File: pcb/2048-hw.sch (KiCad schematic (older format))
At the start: 41 parts

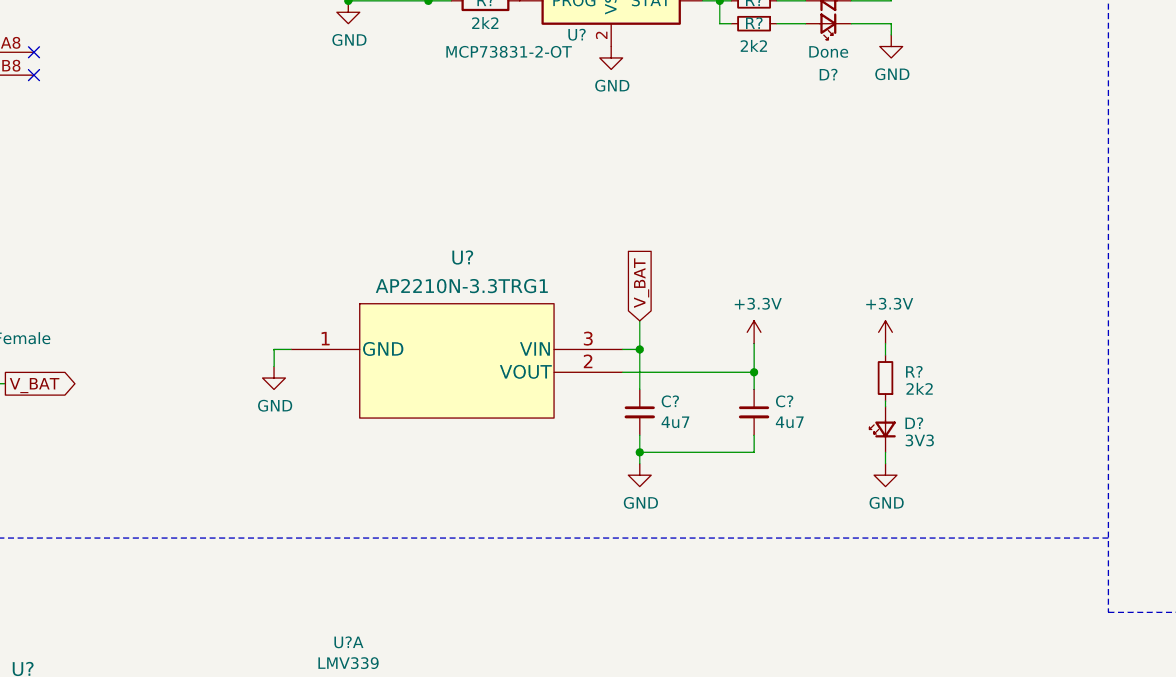
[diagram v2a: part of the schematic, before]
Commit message: Add battery ADC voltage divider
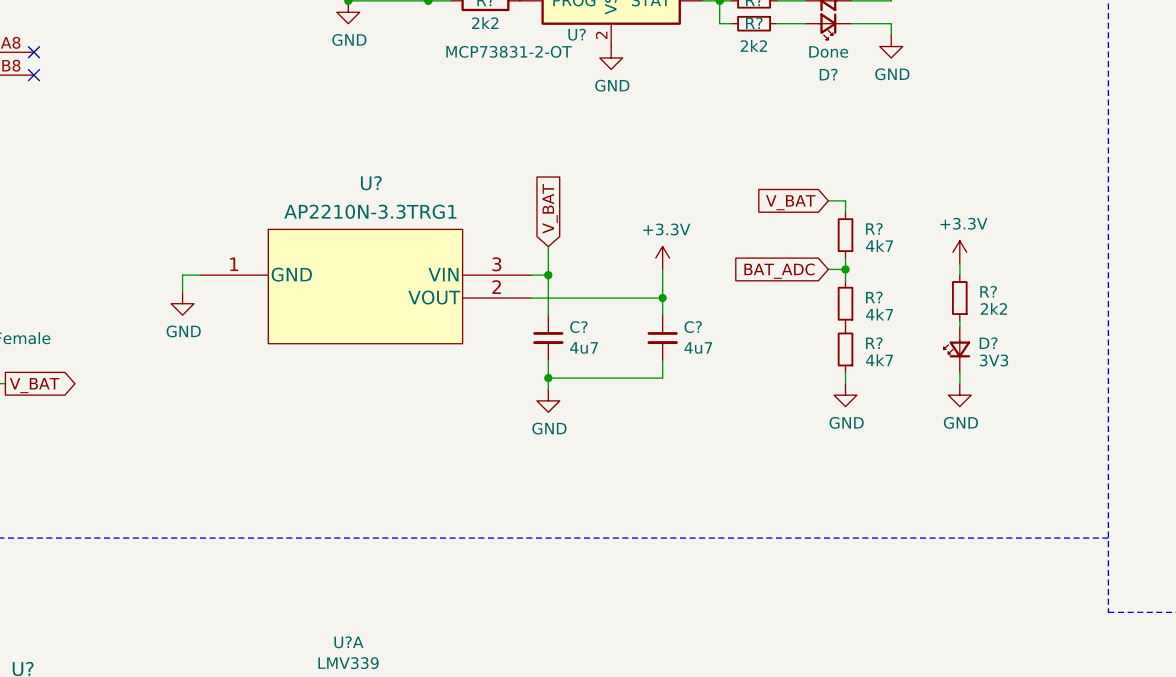
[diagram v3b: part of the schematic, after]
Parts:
- added R? (x3): 4k7, symbol Device:R_Small
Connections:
- net BAT_ADC: now also R?.1, R?.2
- net GND: now also R?.1
- net V_BAT: now also R?.2
- new net: R?.1, R?.2
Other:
- moved on the sheet: C?, D?, R?, U?
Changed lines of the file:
@@
 	1100 3500 1100 3800
 Wire Wire Line
-	2975 3500 2975 3575
-Wire Wire Line
-	3050 3500 2975 3500
-Connection ~ 5075 3600
-Wire Wire Line
-	5075 3600 5075 3475
-Wire Wire Line
-	4575 3950 4575 4000
-Connection ~ 4575 3950
-Wire Wire Line
-	5075 3875 5075 3950
-Wire Wire Line
-	5075 3950 4575 3950
-Wire Wire Line
-	5075 3600 5075 3675
-Wire Wire Line
-	4500 3600 5075 3600
-Wire Wire Line
-	4575 3875 4575 3950
-Wire Wire Line
-	4575 3500 4575 3675
-Wire Wire Line
-	4500 3500 4575 3500
+	2575 3175 2575 3250
+Wire Wire Line
+	2650 3175 2575 3175
+Connection ~ 4675 3275
+Wire Wire Line
+	4675 3275 4675 3150
+Wire Wire Line
+	4175 3625 4175 3675
+Connection ~ 4175 3625
+Wire Wire Line
+	4675 3550 4675 3625
+Wire Wire Line
+	4675 3625 4175 3625
+Wire Wire Line
+	4675 3275 4675 3350
+Wire Wire Line
+	4100 3275 4675 3275
+Wire Wire Line
+	4175 3550 4175 3625
+Wire Wire Line
+	4175 3175 4175 3350
+Wire Wire Line
+	4100 3175 4175 3175
 $Comp
 L power:+3.3V #PWR0112
 U 1 1 5FEF81B7
-P 5075 3475
-F 0 "#PWR0112" H 5075 3325 50  0001 C CNN
-F 1 "+3.3V" H 5090 3648 50  0000 C CNN
-F 2 "" H 5075 3475 50  0001 C CNN
-F 3 "" H 5075 3475 50  0001 C CNN
-	1    5075 3475
+P 4675 3150
+F 0 "#PWR0112" H 4675 3000 50  0001 C CNN
+F 1 "+3.3V" H 4690 3323 50  0000 C CNN
+F 2 "" H 4675 3150 50  0001 C CNN
+F 3 "" H 4675 3150 50  0001 C CNN
+	1    4675 3150
 	1    0    0    -1
 $EndComp
@@
 L power:GND #PWR0113
 U 1 1 5FEF771E
-P 4575 4000
-F 0 "#PWR0113" H 4575 3750 50  0001 C CNN
-F 1 "GND" H 4580 3827 50  0000 C CNN
-F 2 "" H 4575 4000 50  0001 C CNN
-F 3 "" H 4575 4000 50  0001 C CNN
-	1    4575 4000
+P 4175 3675
+F 0 "#PWR0113" H 4175 3425 50  0001 C CNN
+F 1 "GND" H 4180 3502 50  0000 C CNN
+F 2 "" H 4175 3675 50  0001 C CNN
+F 3 "" H 4175 3675 50  0001 C CNN
+	1    4175 3675
 	1    0    0    -1
 $EndComp
@@
 L Device:C_Small C?
 U 1 1 5FEF733E
-P 5075 3775
-F 0 "C?" H 5167 3821 50  0000 L CNN
-F 1 "4u7" H 5167 3730 50  0000 L CNN
-F 2 "" H 5075 3775 50  0001 C CNN
-F 3 "~" H 5075 3775 50  0001 C CNN
-	1    5075 3775
+P 4675 3450
+F 0 "C?" H 4767 3496 50  0000 L CNN
+F 1 "4u7" H 4767 3405 50  0000 L CNN
+F 2 "" H 4675 3450 50  0001 C CNN
+F 3 "~" H 4675 3450 50  0001 C CNN
+	1    4675 3450
 	1    0    0    -1
 $EndComp
@@
 L Device:C_Small C?
 U 1 1 5FEF6AD9
-P 4575 3775
-F 0 "C?" H 4667 3821 50  0000 L CNN
-F 1 "4u7" H 4667 3730 50  0000 L CNN
-F 2 "" H 4575 3775 50  0001 C CNN
-F 3 "~" H 4575 3775 50  0001 C CNN
-	1    4575 3775
+P 4175 3450
+F 0 "C?" H 4267 3496 50  0000 L CNN
+F 1 "4u7" H 4267 3405 50  0000 L CNN
+F 2 "" H 4175 3450 50  0001 C CNN
+F 3 "~" H 4175 3450 50  0001 C CNN
+	1    4175 3450
 	1    0    0    -1
 $EndComp
@@
 L power:GND #PWR0114
 U 1 1 5FEF6103
-P 2975 3575
-F 0 "#PWR0114" H 2975 3325 50  0001 C CNN
-F 1 "GND" H 2980 3402 50  0000 C CNN
-F 2 "" H 2975 3575 50  0001 C CNN
-F 3 "" H 2975 3575 50  0001 C CNN
-	1    2975 3575
+P 2575 3250
+F 0 "#PWR0114" H 2575 3000 50  0001 C CNN
+F 1 "GND" H 2580 3077 50  0000 C CNN
+F 2 "" H 2575 3250 50  0001 C CNN
+F 3 "" H 2575 3250 50  0001 C CNN
+	1    2575 3250
 	1    0    0    -1
 $EndComp
@@
 L ap2210:AP2210N-3.3TRG1 U?
 U 1 1 5FEF5741
-P 3050 3500
-F 0 "U?" H 3800 3900 60  0000 C CNN
-F 1 "AP2210N-3.3TRG1" H 3800 3775 60  0000 C CNN
-F 2 "SOT_3.3TRG1_DIO" H 3850 3740 60  0001 C CNN
-F 3 "" H 3050 3500 60  0000 C CNN
-	1    3050 3500
+P 2650 3175
+F 0 "U?" H 3400 3575 60  0000 C CNN
+F 1 "AP2210N-3.3TRG1" H 3400 3450 60  0000 C CNN
+F 2 "SOT_3.3TRG1_DIO" H 3450 3415 60  0001 C CNN
+F 3 "" H 2650 3175 60  0000 C CNN
+	1    2650 3175
 	1    0    0    -1
 $EndComp
@@
 L power:+3.3V #PWR0115
 U 1 1 5FF1A477
-P 5650 3475
-F 0 "#PWR0115" H 5650 3325 50  0001 C CNN
-F 1 "+3.3V" H 5665 3648 50  0000 C CNN
-F 2 "" H 5650 3475 50  0001 C CNN
-F 3 "" H 5650 3475 50  0001 C CNN
-	1    5650 3475
+P 5975 3125
+F 0 "#PWR0115" H 5975 2975 50  0001 C CNN
+F 1 "+3.3V" H 5990 3298 50  0000 C CNN
+F 2 "" H 5975 3125 50  0001 C CNN
+F 3 "" H 5975 3125 50  0001 C CNN
+	1    5975 3125
 	1    0    0    -1
 $EndComp
@@
 L Device:R_Small R?
 U 1 1 5FF1A977
-P 5650 3625
-F 0 "R?" H 5525 3600 50  0000 C CNN
-F 1 "2k2" H 5500 3675 50  0000 C CNN
-F 2 "" H 5650 3625 50  0001 C CNN
-F 3 "~" H 5650 3625 50  0001 C CNN
-	1    5650 3625
+P 5975 3275
+F 0 "R?" H 5850 3250 50  0000 C CNN
+F 1 "2k2" H 5825 3325 50  0000 C CNN
+F 2 "" H 5975 3275 50  0001 C CNN
+F 3 "~" H 5975 3275 50  0001 C CNN
+	1    5975 3275
 	-1   0    0    1
 $EndComp
@@
 L Device:LED_Small D?
 U 1 1 5FF1B0E2
-P 5650 3850
-F 0 "D?" V 5675 3725 50  0000 C CNN
-F 1 "3V3" V 5600 3700 50  0000 C CNN
-F 2 "" V 5650 3850 50  0001 C CNN
-F 3 "~" V 5650 3850 50  0001 C CNN
-	1    5650 3850
+P 5975 3500
+F 0 "D?" V 6000 3375 50  0000 C CNN
+F 1 "3V3" V 5925 3350 50  0000 C CNN
+F 2 "" V 5975 3500 50  0001 C CNN
+F 3 "~" V 5975 3500 50  0001 C CNN
+	1    5975 3500
 	0    -1   -1   0
 $EndComp
@@
 L power:GND #PWR0116
 U 1 1 5FF1BC0E
-P 5650 4000
-F 0 "#PWR0116" H 5650 3750 50  0001 C CNN
-F 1 "GND" H 5655 3827 50  0000 C CNN
-F 2 "" H 5650 4000 50  0001 C CNN
-F 3 "" H 5650 4000 50  0001 C CNN
-	1    5650 4000
-	1    0    0    -1
-$EndComp
-Text GLabel 4575 3375 1    50   Input ~ 0
+P 5975 3650
+F 0 "#PWR0116" H 5975 3400 50  0001 C CNN
+F 1 "GND" H 5980 3477 50  0000 C CNN
+F 2 "" H 5975 3650 50  0001 C CNN
+F 3 "" H 5975 3650 50  0001 C CNN
+	1    5975 3650
+	1    0    0    -1
+$EndComp
+Text GLabel 4175 3050 1    50   Input ~ 0
 V_BAT
 Wire Wire Line
-	4575 3500 4575 3375
-Connection ~ 4575 3500
-Wire Wire Line
-	5650 3475 5650 3525
-Wire Wire Line
-	5650 3725 5650 3750
-Wire Wire Line
-	5650 3950 5650 4000
+	4175 3175 4175 3050
+Connection ~ 4175 3175
+Wire Wire Line
+	5975 3125 5975 3175
+Wire Wire Line
+	5975 3375 5975 3400
+Wire Wire Line
+	5975 3600 5975 3650
 $Comp
 L MCU_ST_STM32F3:STM32F303K8Tx U?
@@
 Wire Notes Line
 	6625 475  6625 4650
+$Comp
+L Device:R_Small R?
+U 1 1 5FFE2625
+P 5475 3000
+F 0 "R?" H 5350 2975 50  0000 C CNN
+F 1 "4k7" H 5325 3050 50  0000 C CNN
+F 2 "" H 5475 3000 50  0001 C CNN
+F 3 "~" H 5475 3000 50  0001 C CNN
+	1    5475 3000
+	-1   0    0    1
+$EndComp
+$Comp
+L power:GND #PWR?
+U 1 1 5FFE2631
+P 5475 3650
+F 0 "#PWR?" H 5475 3400 50  0001 C CNN
+F 1 "GND" H 5480 3477 50  0000 C CNN
+F 2 "" H 5475 3650 50  0001 C CNN
+F 3 "" H 5475 3650 50  0001 C CNN
+	1    5475 3650
+	1    0    0    -1
+$EndComp
+$Comp
+L Device:R_Small R?
+U 1 1 5FFEB48F
+P 5475 3300
+F 0 "R?" H 5350 3275 50  0000 C CNN
+F 1 "4k7" H 5325 3350 50  0000 C CNN
+F 2 "" H 5475 3300 50  0001 C CNN
+F 3 "~" H 5475 3300 50  0001 C CNN
+	1    5475 3300
+	-1   0    0    1
+$EndComp
+$Comp
+L Device:R_Small R?
+U 1 1 5FFEB927
+P 5475 3500
+F 0 "R?" H 5350 3475 50  0000 C CNN
+F 1 "4k7" H 5325 3550 50  0000 C CNN
+F 2 "" H 5475 3500 50  0001 C CNN
+F 3 "~" H 5475 3500 50  0001 C CNN
+	1    5475 3500
+	-1   0    0    1
+$EndComp
+Wire Wire Line
+	5475 3650 5475 3600
+Wire Wire Line
+	5475 3100 5475 3150
+Text GLabel 5400 2850 0    50   Input ~ 0
+V_BAT
+Text GLabel 5400 3150 0    50   Input ~ 0
+BAT_ADC
+Wire Wire Line
+	5400 2850 5475 2850
+Wire Wire Line
+	5400 3150 5475 3150
+Connection ~ 5475 3150
+Wire Wire Line
+	5475 3150 5475 3200
+Wire Wire Line
+	5475 2850 5475 2900
 $EndSCHEMATC

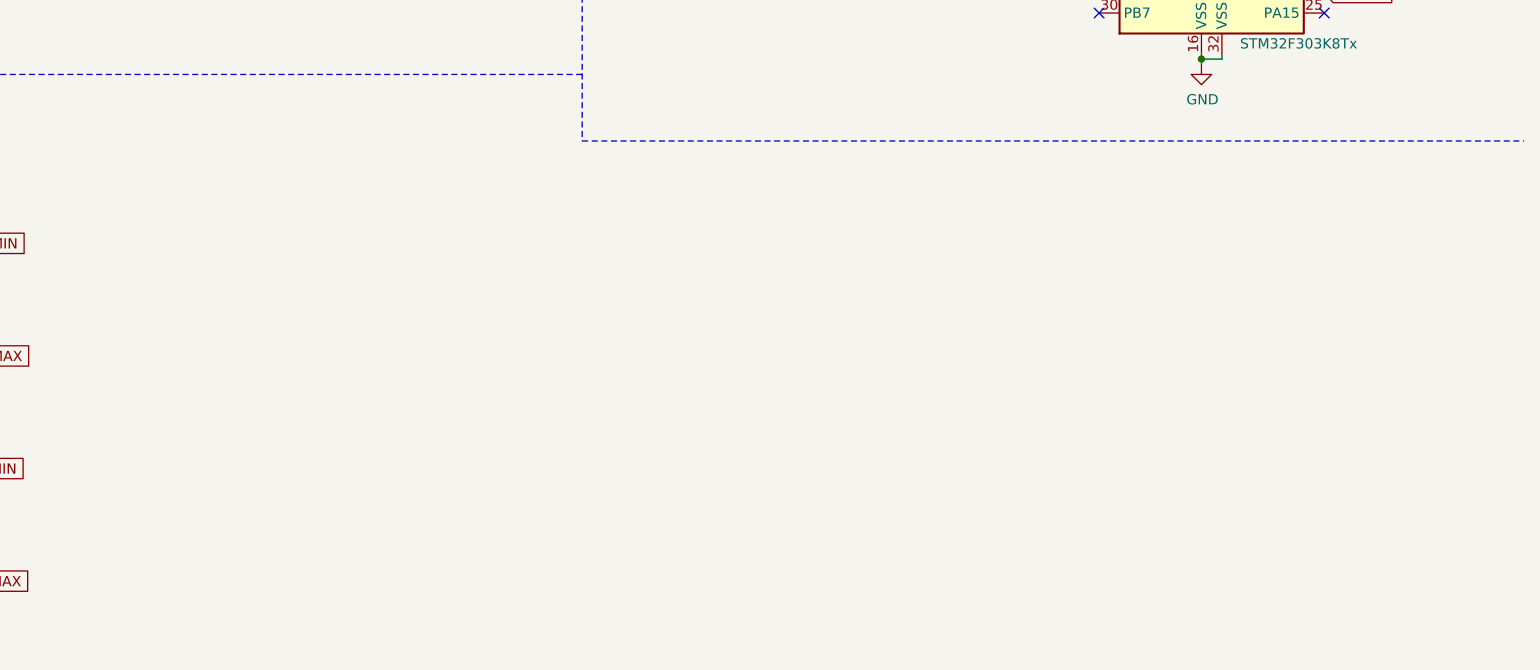
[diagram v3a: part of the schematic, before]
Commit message: Add ws2812b LEDs
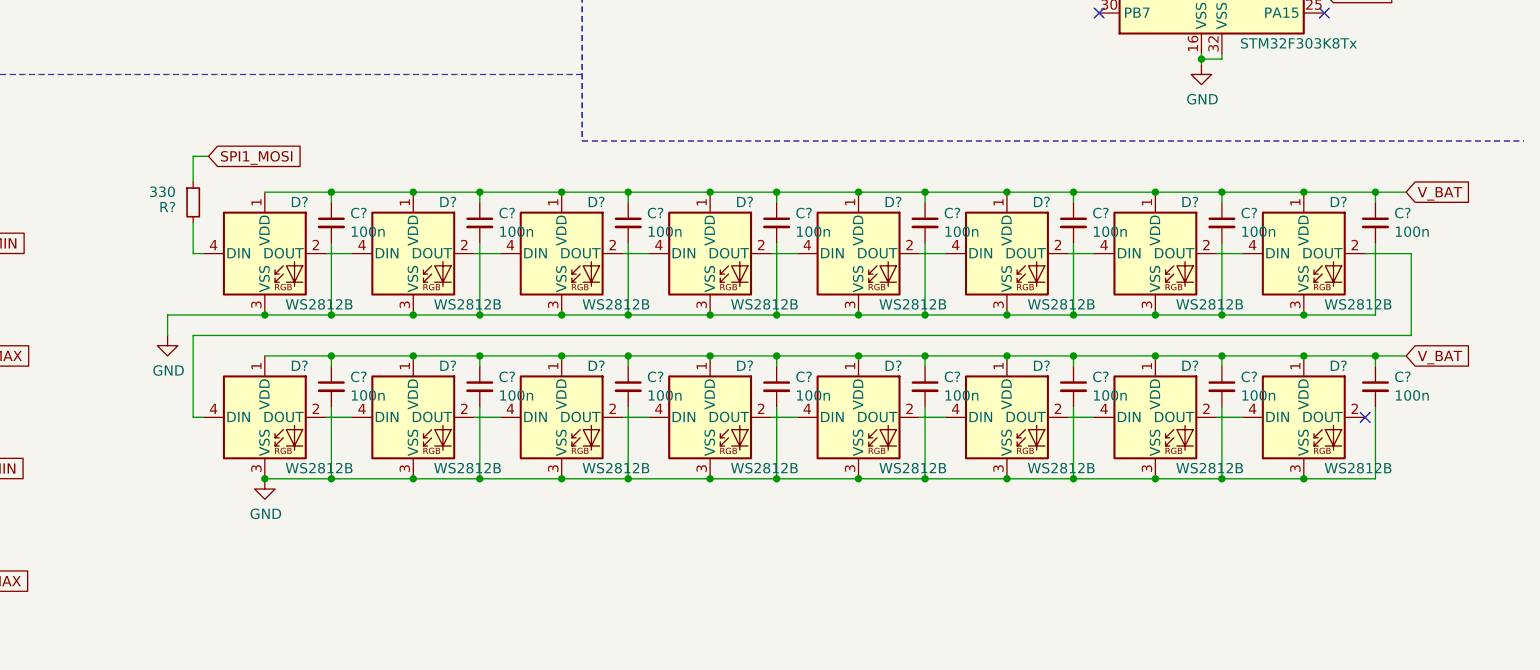
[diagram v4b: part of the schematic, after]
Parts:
- added C? (x16): 100n, symbol Device:C_Small
- added D? (x16): WS2812B, LED_SMD:LED_WS2812B_PLCC4_5.0x5.0mm_P3.2mm, symbol LED:WS2812B
- added R?: 330, symbol Device:R_Small
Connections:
- net GND: now also C?.2, C?.2, C?.2, C?.2, C?.2, C?.2, C?.2, C?.2, C?.2, C?.2, C?.2, C?.2, C?.2, C?.2, C?.2, C?.2, D?.3 (VSS), D?.3 (VSS), D?.3 (VSS), D?.3 (VSS), D?.3 (VSS), D?.3 (VSS), D?.3 (VSS), D?.3 (VSS), D?.3 (VSS), D?.3 (VSS), D?.3 (VSS), D?.3 (VSS), D?.3 (VSS), D?.3 (VSS), D?.3 (VSS), D?.3 (VSS)
- net SPI1_MOSI: now also R?.1
- net V_BAT: now also C?.1, C?.1, C?.1, C?.1, C?.1, C?.1, C?.1, C?.1, C?.1, C?.1, C?.1, C?.1, C?.1, C?.1, C?.1, C?.1, D?.1 (VDD), D?.1 (VDD), D?.1 (VDD), D?.1 (VDD), D?.1 (VDD), D?.1 (VDD), D?.1 (VDD), D?.1 (VDD), D?.1 (VDD), D?.1 (VDD), D?.1 (VDD), D?.1 (VDD), D?.1 (VDD), D?.1 (VDD), D?.1 (VDD), D?.1 (VDD)
- new net: D?.2 (DOUT), D?.4 (DIN) (x15)
- new net: D?.4 (DIN), R?.2
- no-connect marks 13 -> 14

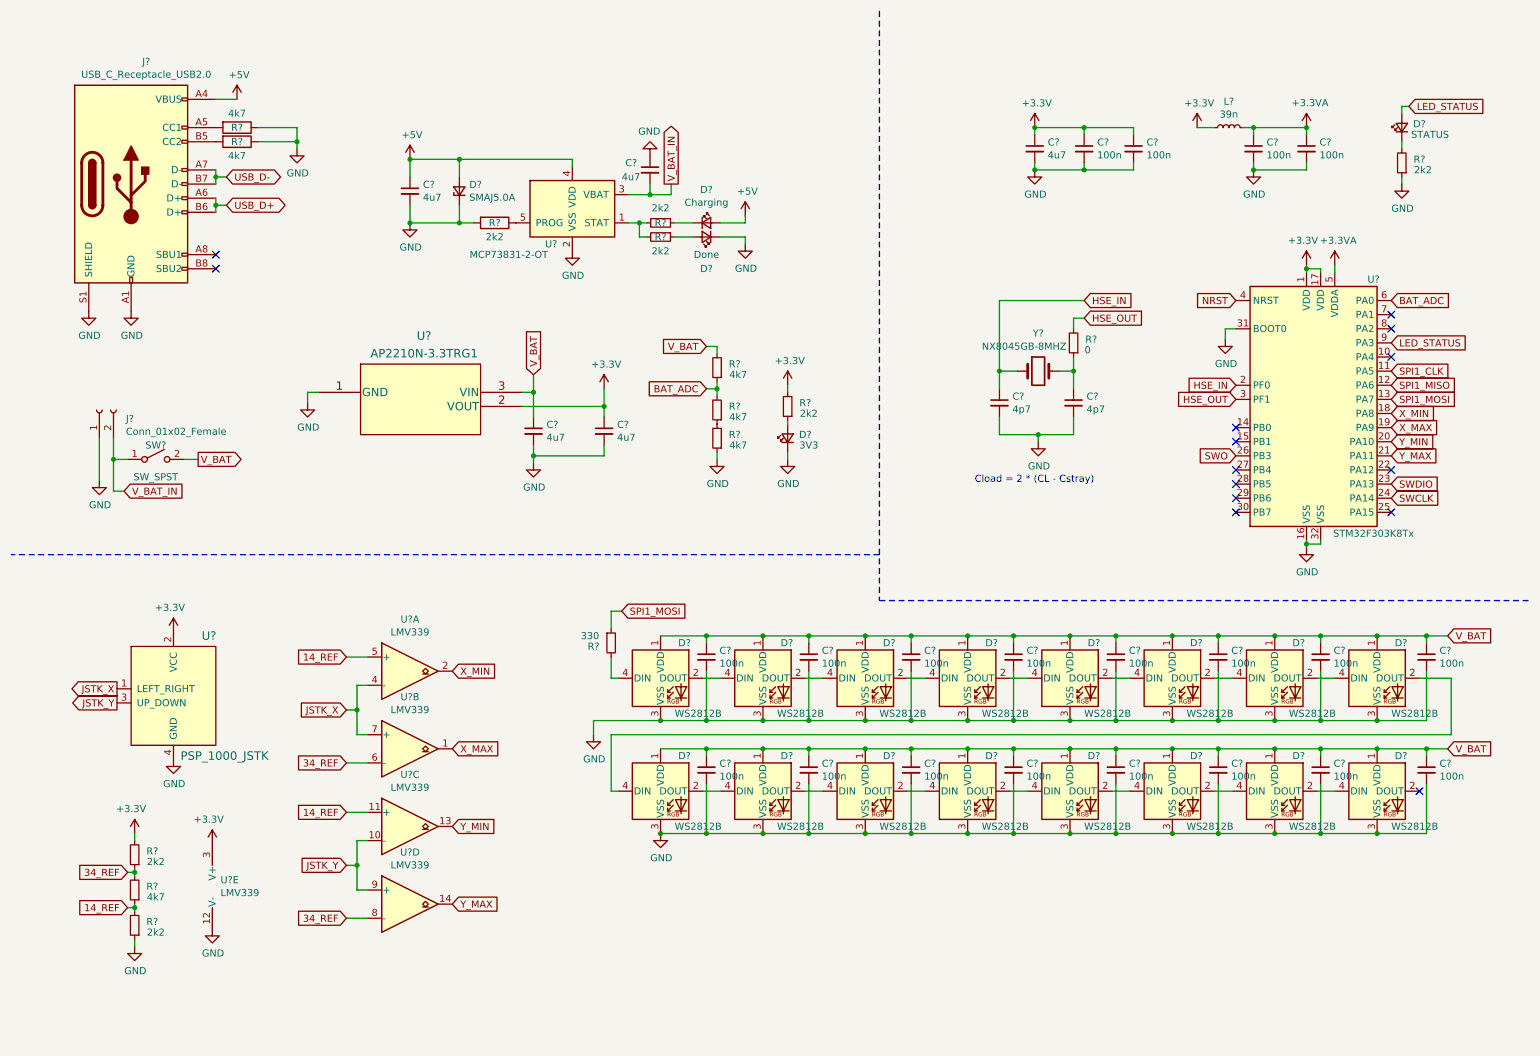
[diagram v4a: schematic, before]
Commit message: Add SWD header
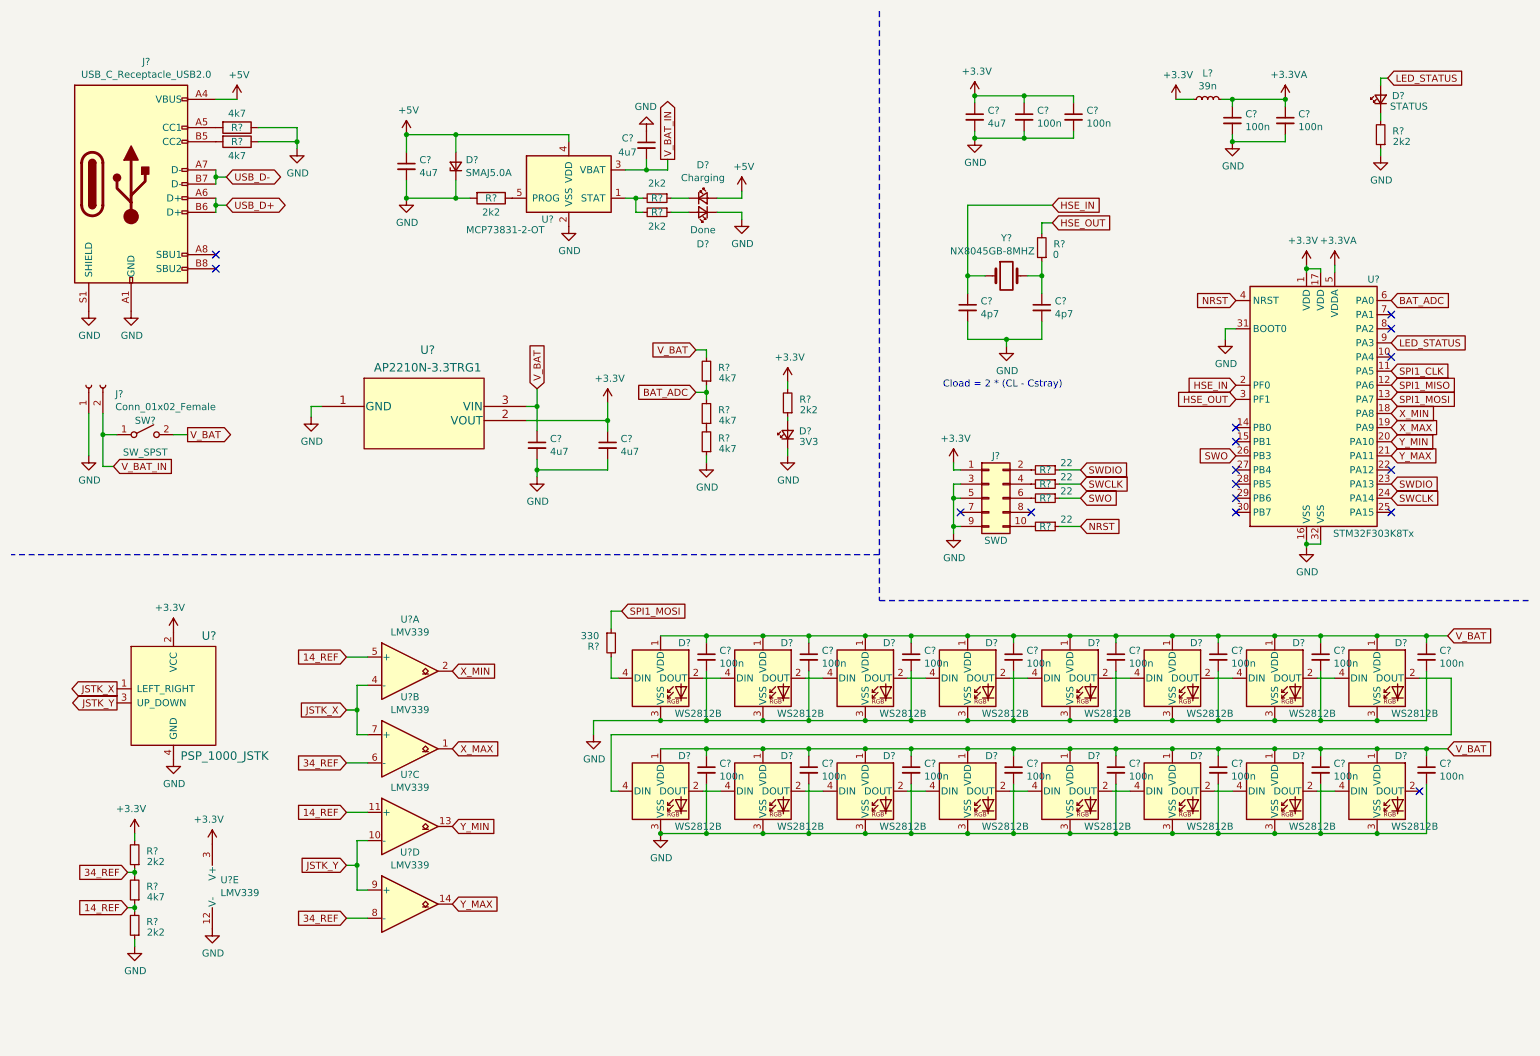
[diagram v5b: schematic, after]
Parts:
- added J?: SWD, symbol Connector_Generic:Conn_02x05_Odd_Even
- added R? (x4): 22, symbol Device:R_Small
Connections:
- net +3V3: now also J?.1 (Pin_1)
- net GND: now also J?.3 (Pin_3), J?.5 (Pin_5), J?.9 (Pin_9)
- net NRST: now also R?.1
- net SWCLK: now also R?.1
- net SWDIO: now also R?.1
- net SWO: now also R?.1
- new net: J?.10 (Pin_10), R?.2
- new net: J?.2 (Pin_2), R?.2
- new net: J?.4 (Pin_4), R?.2
- new net: J?.6 (Pin_6), R?.2
- no-connect marks 14 -> 16
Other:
- moved on the sheet: C?, D?, J?, L?, R?, SW?, U?, Y?
